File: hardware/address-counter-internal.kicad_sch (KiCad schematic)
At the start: 10 parts, among them U3 74LV161A, U4 74LV161A, U5 74LV161A, U6 74LV161A, U7 74LV161A

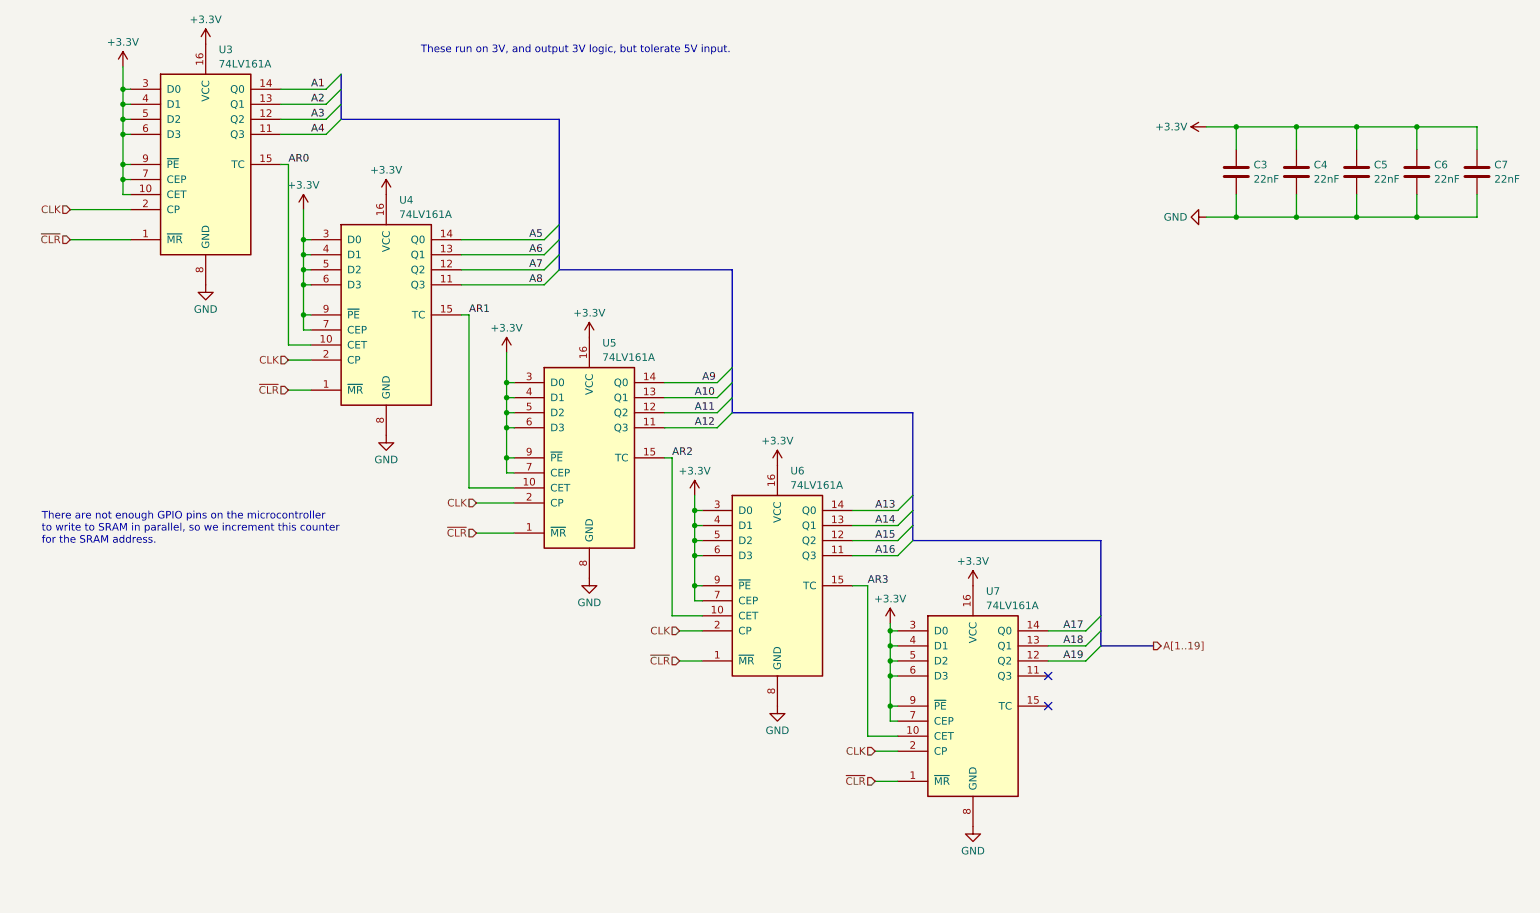
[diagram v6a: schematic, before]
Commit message: Move microcontroller board design into shareable subsheet
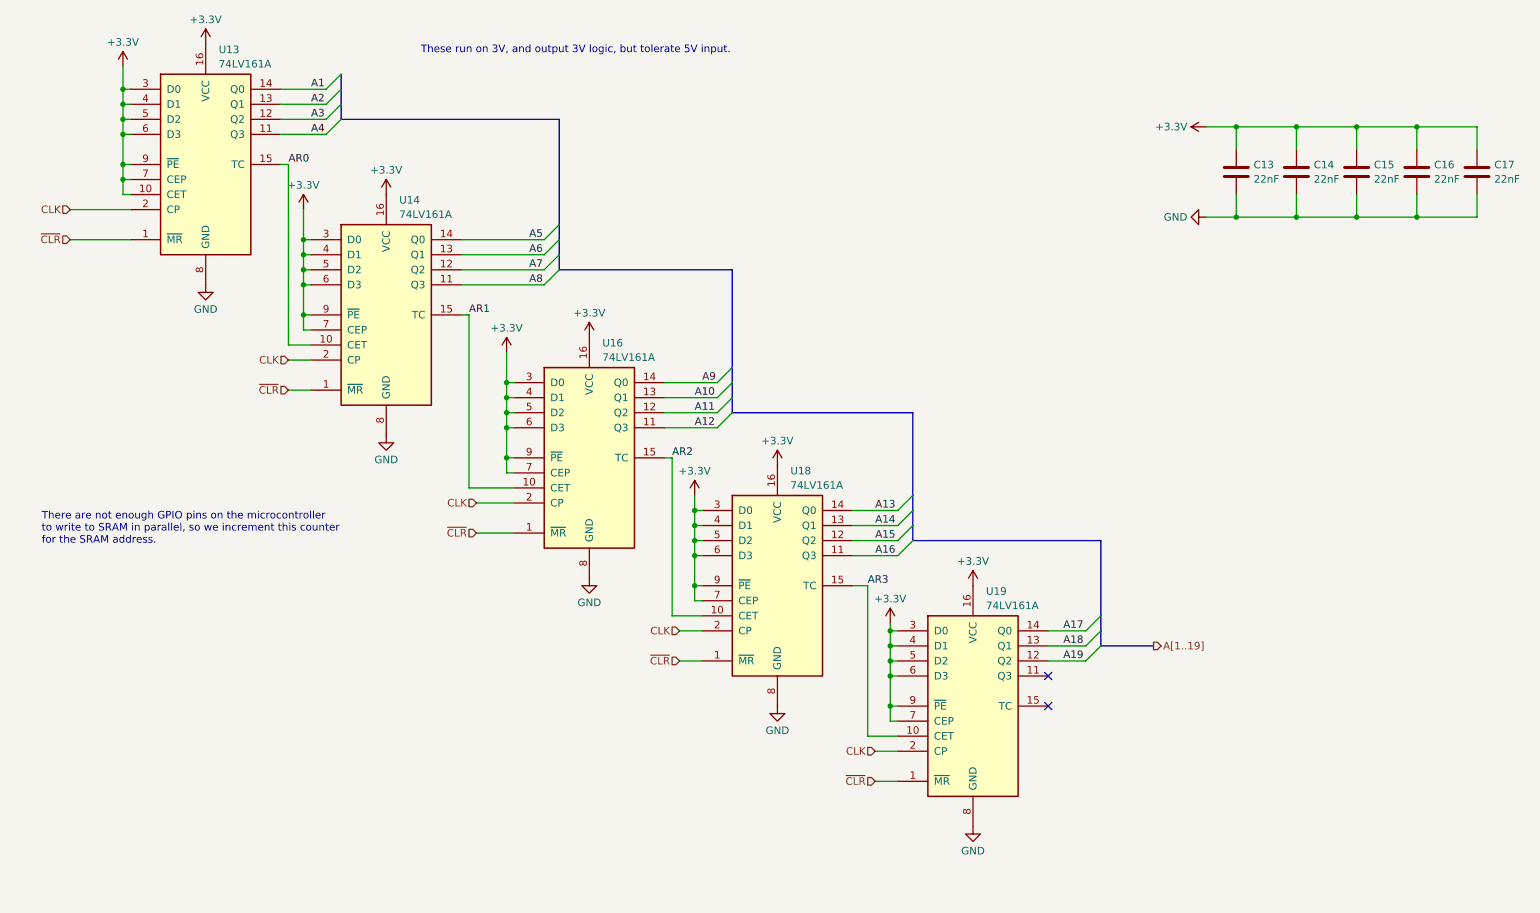
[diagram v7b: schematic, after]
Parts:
- renumbered C3 to C13, C4 to C14, C5 to C15, C6 to C16, C7 to C17, U3 to U13, U4 to U14, U5 to U16, U6 to U18, U7 to U19

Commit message: Reannotate schematics and drop debug bridges
Parts are now numbered starting at 0 for cart, 100 for SRAM, 300 for
microcontroller.

Also, drop debug bridges that made routing more difficult and had the
same names across prototype boards.

Hopefully this will help avoid naming conflicts for the unified PCB.

Also, redo prototype PCB layouts.

Now that all the names have changed, update board layouts.
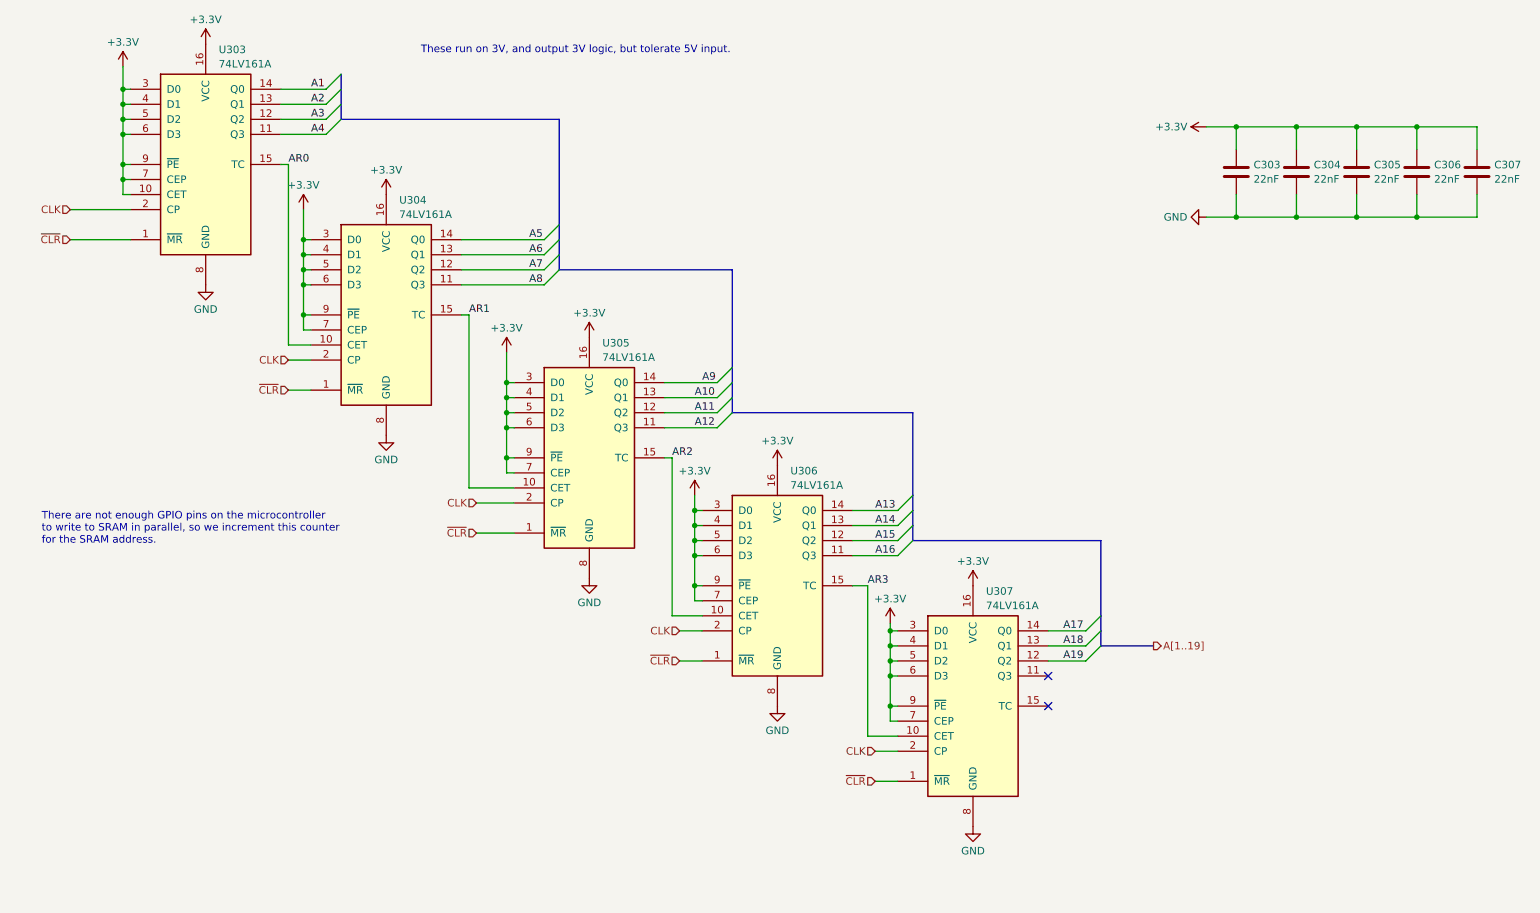
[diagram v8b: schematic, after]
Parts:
- renumbered C13 to C303, C14 to C304, C15 to C305, C16 to C306, C17 to C307, U13 to U303, U14 to U304, U16 to U305, U18 to U306, U19 to U307
